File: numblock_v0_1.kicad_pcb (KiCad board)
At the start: 2 copper layers, 100 x 100 mm, 159 parts, among them J1 Conn_01x14_Female, J2 Conn_01x14_Female, J3 Conn_01x05_Female, SW1 SW_PUSH-MX_W_LED, SW10 SW_PUSH-MX_W_LED, SW11 SW_PUSH-MX_W_LED, SW12 SW_PUSH-MX_W_LED, SW13 SW_PUSH-MX_W_LED, SW14 SW_PUSH-MX_W_LED, SW15 SW_PUSH-MX_W_LED, SW16 SW_PUSH-MX_W_LED, SW17 SW_PUSH-MX_W_LED, SW18 SW_PUSH-MX_W_LED, SW19 SW_PUSH-MX_W_LED, SW2 SW_PUSH-MX_W_LED, SW20 SW_PUSH-MX_W_LED, SW21 Rotary_Encoder_Switch, SW22 Rotary_Encoder_Switch, SW3 SW_PUSH-MX_W_LED, SW4 SW_PUSH-MX_W_LED, SW5 SW_PUSH-MX_W_LED, SW6 SW_PUSH-MX_W_LED, SW7 SW_PUSH-MX_W_LED, SW8 SW_PUSH-MX_W_LED, SW9 SW_PUSH-MX_W_LED

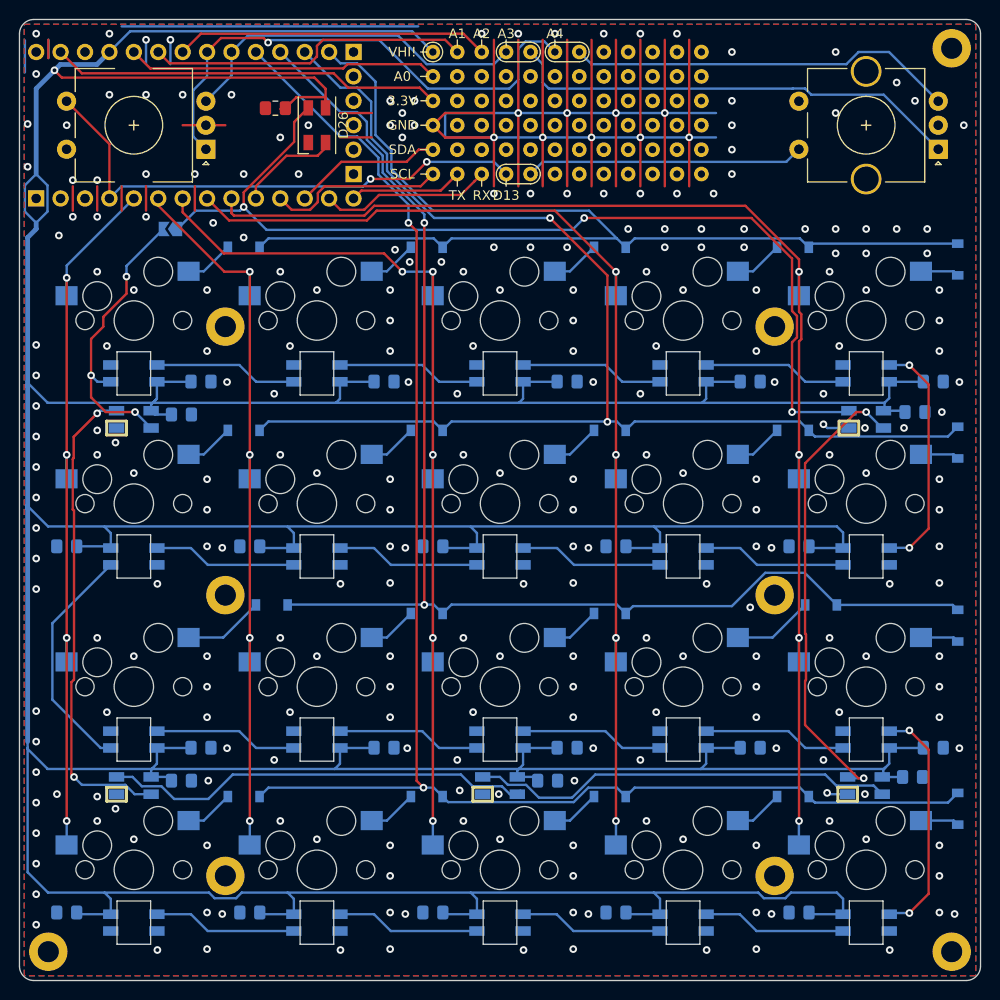
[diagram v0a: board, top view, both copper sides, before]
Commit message: mounting holes added
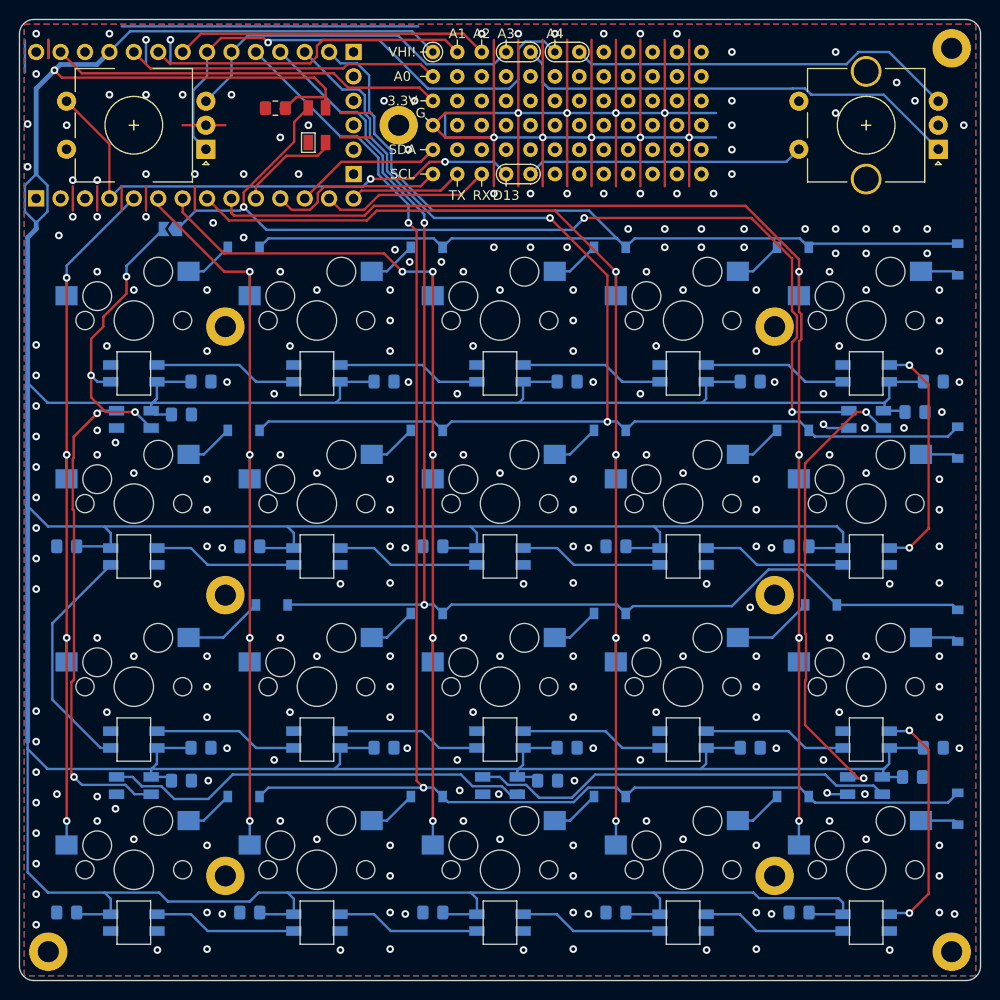
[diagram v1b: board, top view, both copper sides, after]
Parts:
- added TH1: HOLE, sofle:M2_HOLE_PCB, F.Cu at (65.7, 36.8)
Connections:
- TH1 pad : (no net) -> GND (x9)
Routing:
- net GND: vias 268 -> 265
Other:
- board text added: "G"
- board text removed: "GND"

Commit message: replaced plated mountig holes to unplated; final touches before placing order
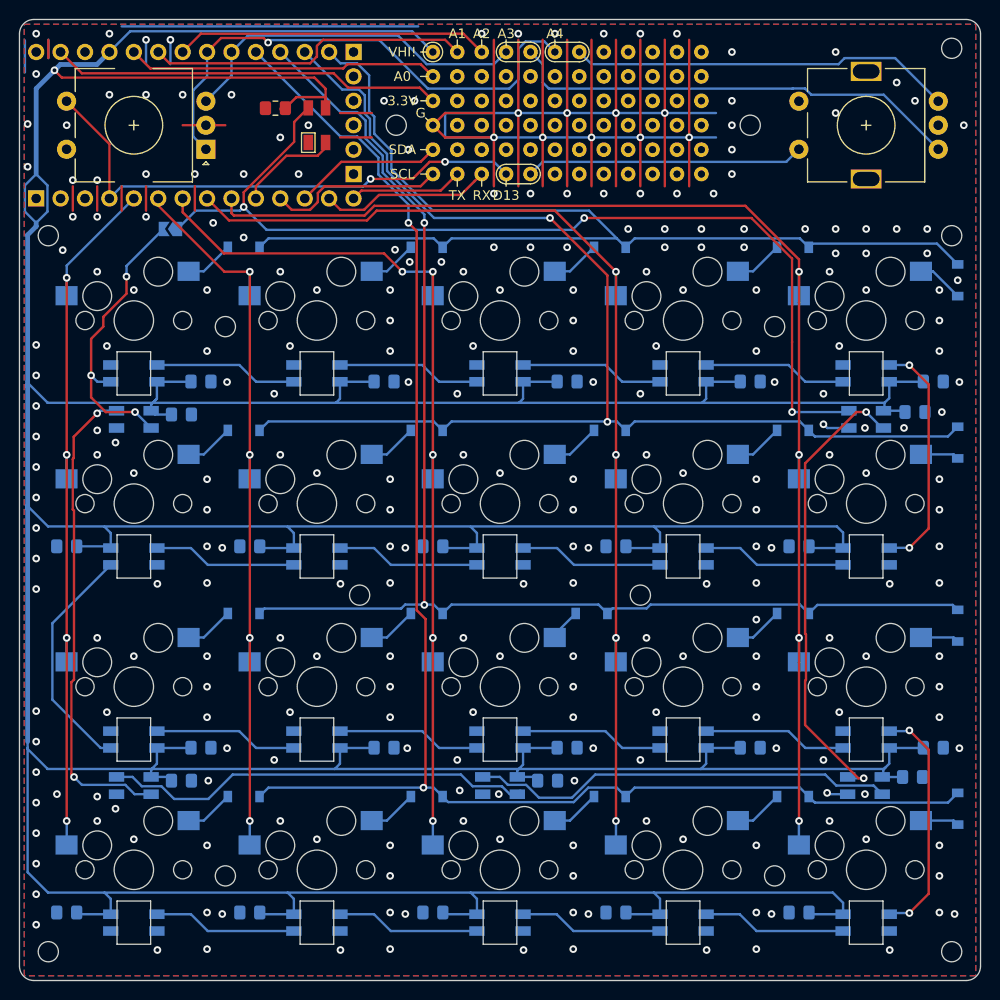
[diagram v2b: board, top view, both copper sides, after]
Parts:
- removed the TH1 at (65.7, 36.8)
- removed the TH1 at (104.8, 85.7)
- removed the TH1 at (47.6, 85.7)
- removed the TH1 at (47.6, 57.8)
- removed the TH1 at (104.8, 57.8)
- removed the TH1 at (104.8, 114.9)
- removed the TH1 at (47.6, 114.9)
- removed the TH1 at (29.2, 122.8)
- removed the TH1 at (123.2, 122.8)
- added G***: LOGO, general:by, B.Cu at (40.6, 36.2)
- added G***: LOGO, general:jk_large, B.Cu at (36.2, 36.8)
- added TH1: HOLE, MountingHole:MountingHole_2.1mm, F.Cu at (61.6, 85.7)
- added TH1: HOLE, MountingHole:MountingHole_2.1mm, F.Cu at (29.2, 48.3)
- added TH1: HOLE, MountingHole:MountingHole_2.1mm, F.Cu at (29.2, 122.8)
- added TH1: HOLE, MountingHole:MountingHole_2.1mm, F.Cu at (123.2, 122.8)
- added TH1: HOLE, MountingHole:MountingHole_2.1mm, F.Cu at (90.8, 85.7)
- added TH1: HOLE, MountingHole:MountingHole_2.1mm, F.Cu at (104.8, 57.8)
- added TH1: HOLE, MountingHole:MountingHole_2.1mm, F.Cu at (47.6, 57.8)
- added TH1: HOLE, MountingHole:MountingHole_2.1mm, F.Cu at (104.8, 114.9)
- added TH1: HOLE, MountingHole:MountingHole_2.1mm, F.Cu at (47.6, 114.9)
- added TH1: HOLE, MountingHole:MountingHole_2.1mm, F.Cu at (102.2, 36.8)
- added TH1: HOLE, MountingHole:MountingHole_2.1mm, F.Cu at (65.4, 36.8)
- added TH1: HOLE, MountingHole:MountingHole_2.1mm, F.Cu at (123.2, 48.3)
- SW22: footprint Rotary_Encoder:RotaryEncoder_Alps_EC11E-Switch_Vertical_H20mm_CircularMountingHoles -> sofle RGB:RotaryEncoder_Alps_EC11E-Switch_Vertical_H20mm-keebio_modified
- TH1: footprint sofle:M2_HOLE_PCB -> MountingHole:MountingHole_2.1mm
- moved D11 3.05 mm to (49.5, 87.6)
- moved D14 3.05 mm to (106.7, 87.6)
- moved D5 2.16 mm to (123.8, 53.0)
- moved D13 1.91 mm to (85.7, 87.6)
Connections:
- TH1 pad : GND -> (no net)
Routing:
- net Net-(D11-Pad1): track 8.40 -> 5.12 mm
- net Net-(D14-Pad1): track 8.40 -> 5.12 mm
- net Net-(D13-Pad1): track 5.12 -> 3.40 mm
- net /R3: track 139.3 -> 140.3 mm
- net /R1: track 117.4 -> 118.3 mm
- net Net-(D5-Pad1): track 4.00 -> 4.89 mm
- net +5V: track 659.7 -> 658.9 mm
- net Net-(H14-Pad1): track 40.5 -> 40.0 mm
- net GND: vias 265 -> 268
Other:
- board text added: "JLCJLCJLCJLC"
